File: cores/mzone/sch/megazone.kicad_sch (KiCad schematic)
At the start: 8 parts

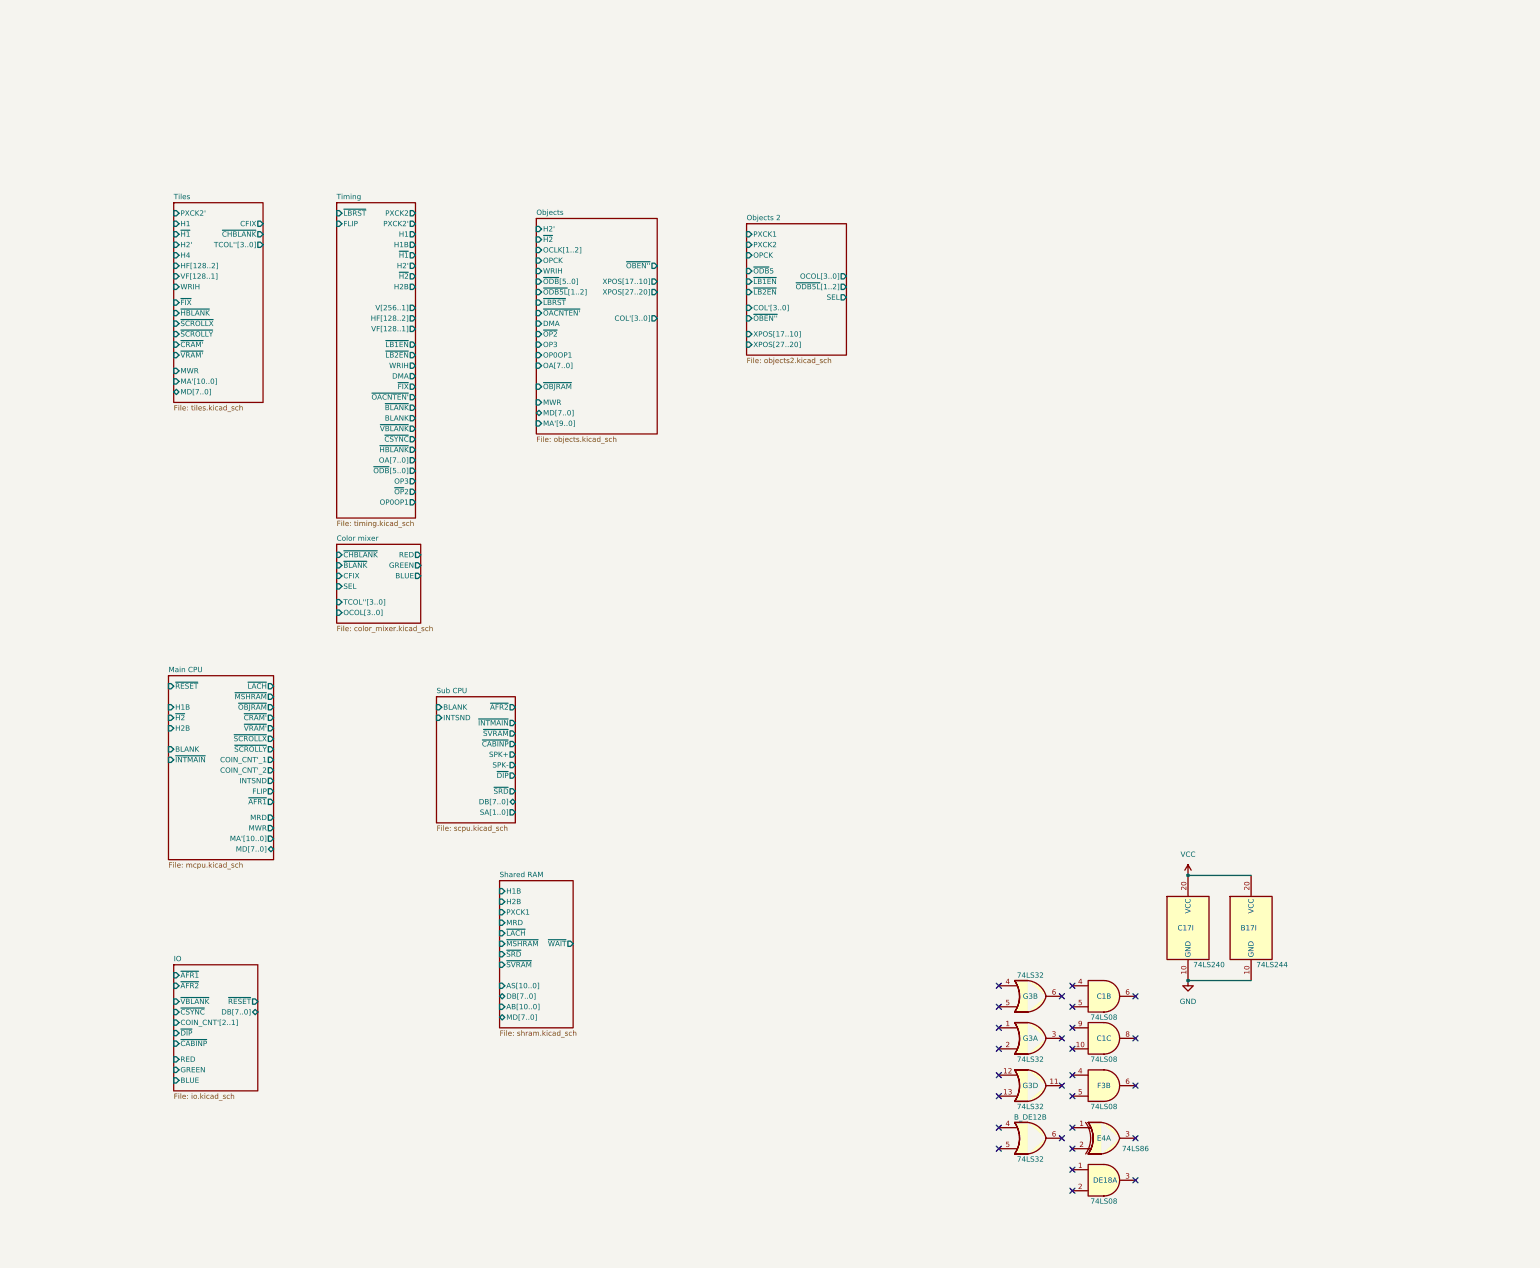
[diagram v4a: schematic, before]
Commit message: mzone core
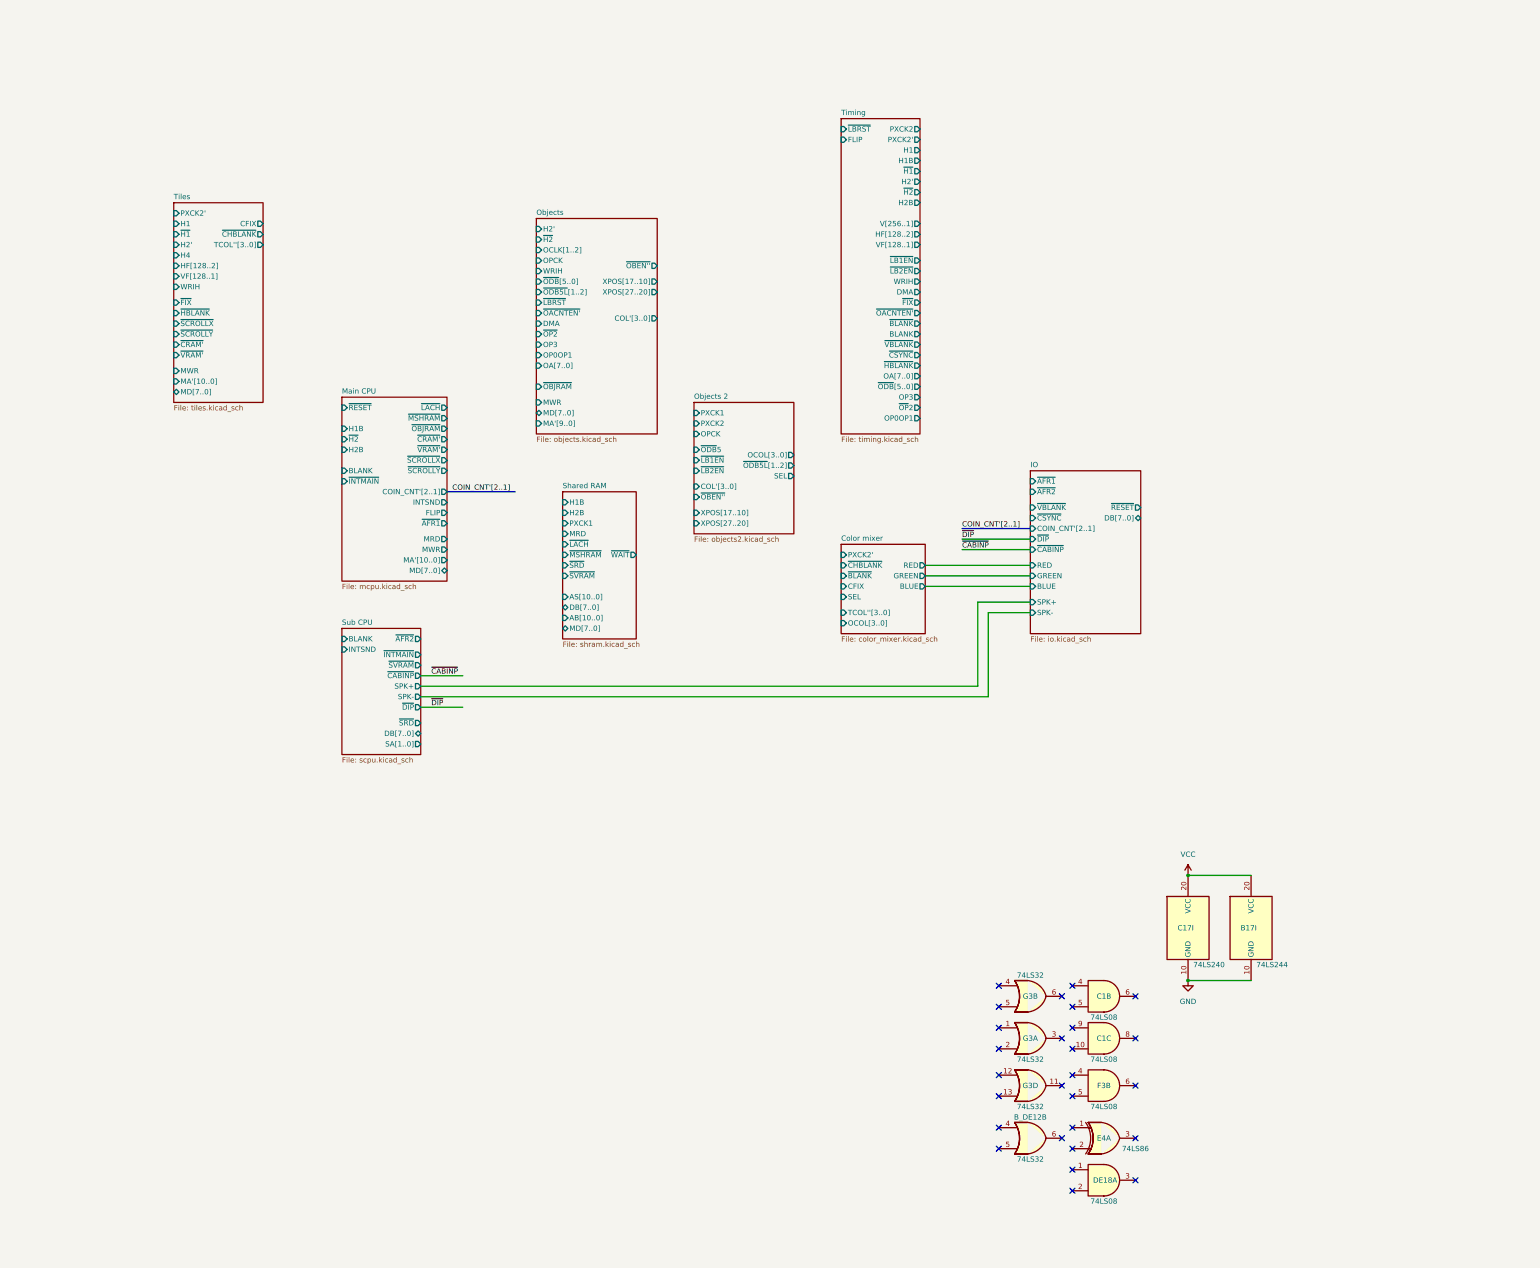
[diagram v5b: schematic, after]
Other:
- sheet Color mixer ports: added PXCK2'; removed none
- sheet IO ports: added SPK+, SPK-; removed none
- sheet Main CPU ports: added COIN_CNT'[2..1]; removed COIN_CNT'_1, COIN_CNT'_2

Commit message: mzone core
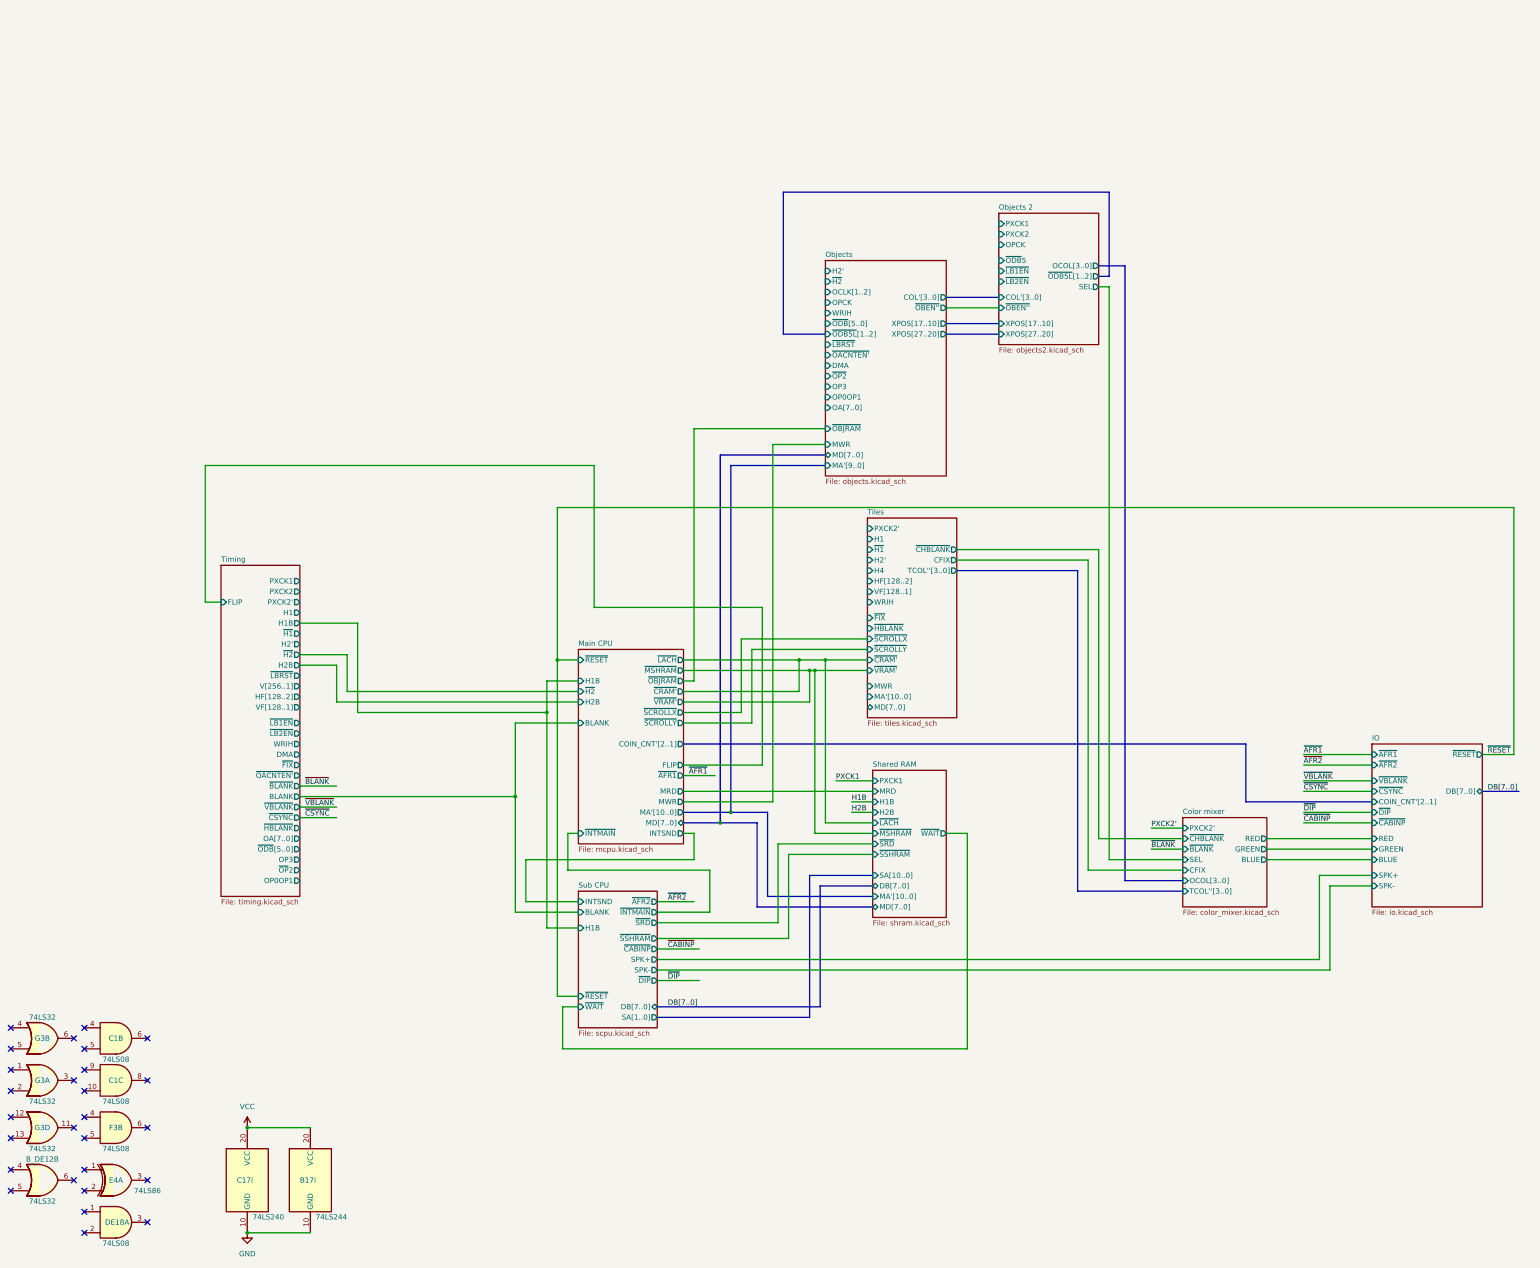
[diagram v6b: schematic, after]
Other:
- sheet Shared RAM ports: added MA'[10..0], SA[10..0], ~{SSHRAM}; removed AB[10..0], AS[10..0], ~{SVRAM}
- sheet Sub CPU ports: added H1B, ~{RESET}, ~{SSHRAM}, ~{WAIT}; removed ~{SVRAM}
- sheet Timing ports: added PXCK1; removed none
- moved on the sheet: B17I, B_DE12B, C17I, C1B, C1C, DE18A, E4A, F3B, G3A, G3B, G3D

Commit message: mzone core
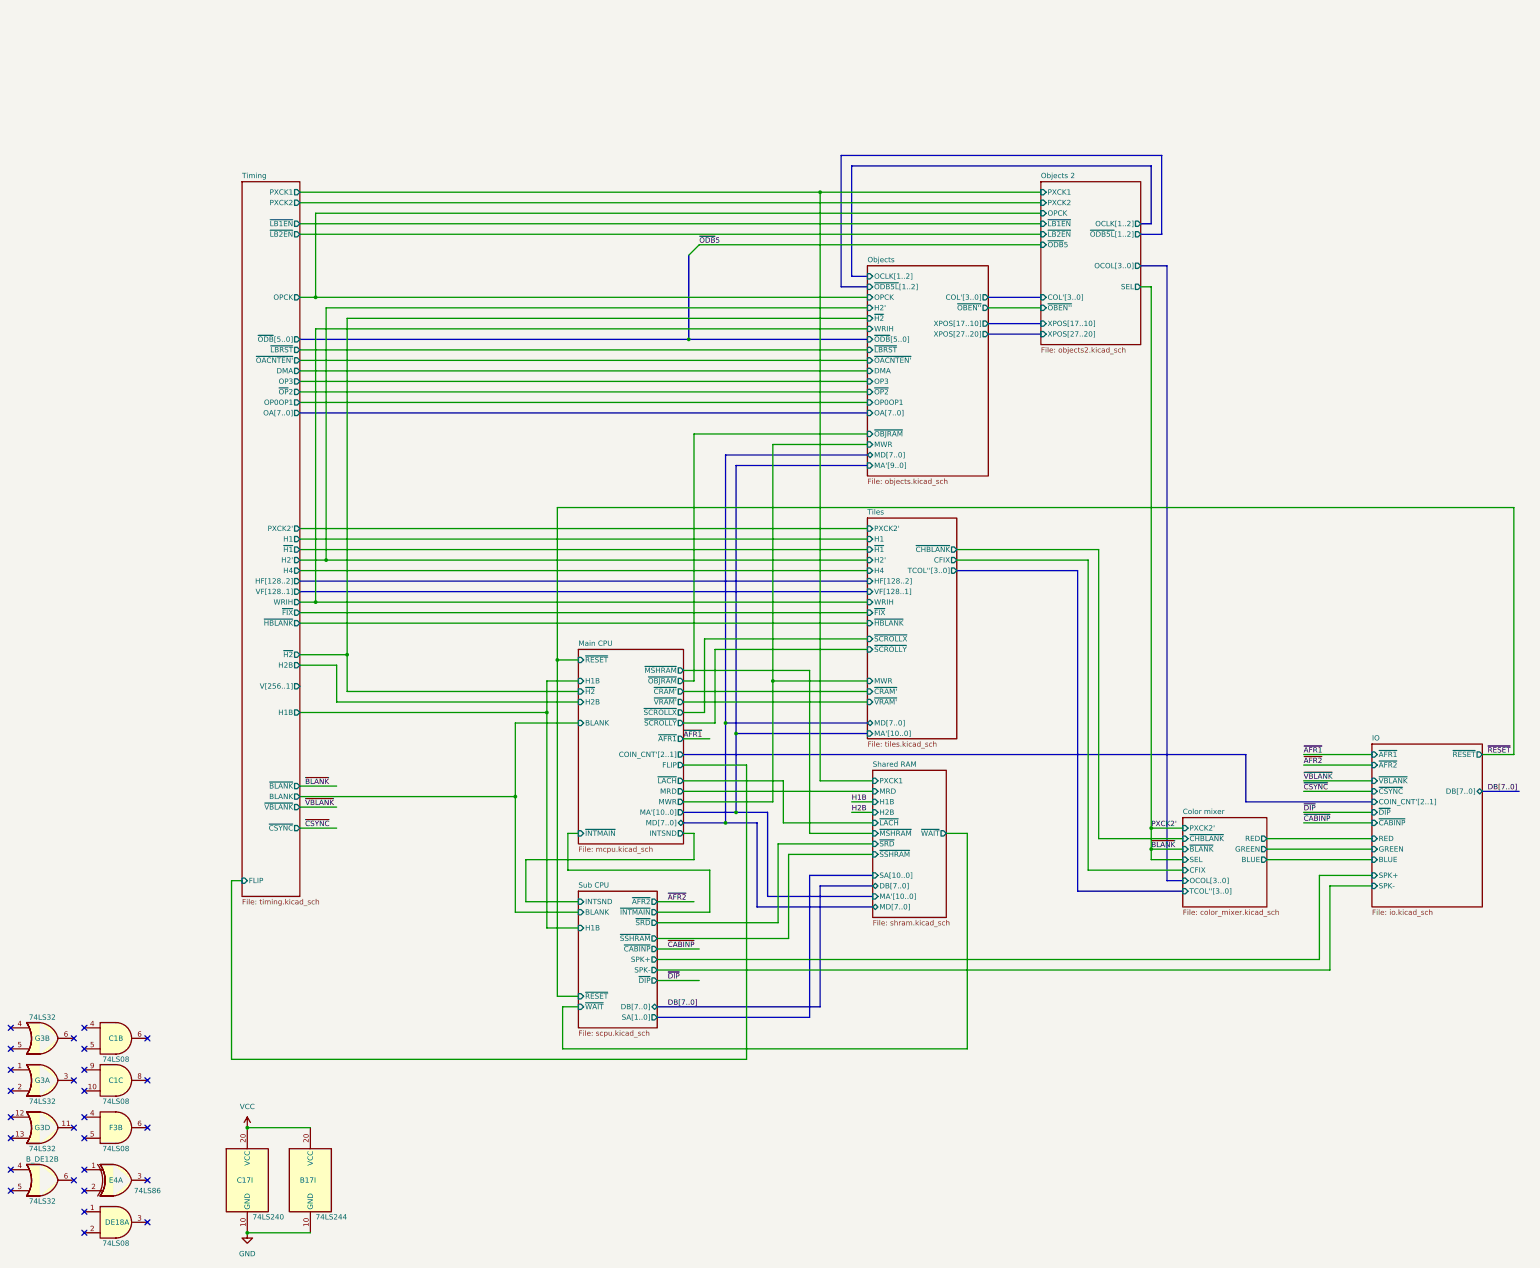
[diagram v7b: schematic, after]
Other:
- sheet Objects 2 ports: added OCLK[1..2]; removed none
- sheet Timing ports: added H4, OPCK; removed none

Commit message: mzone core
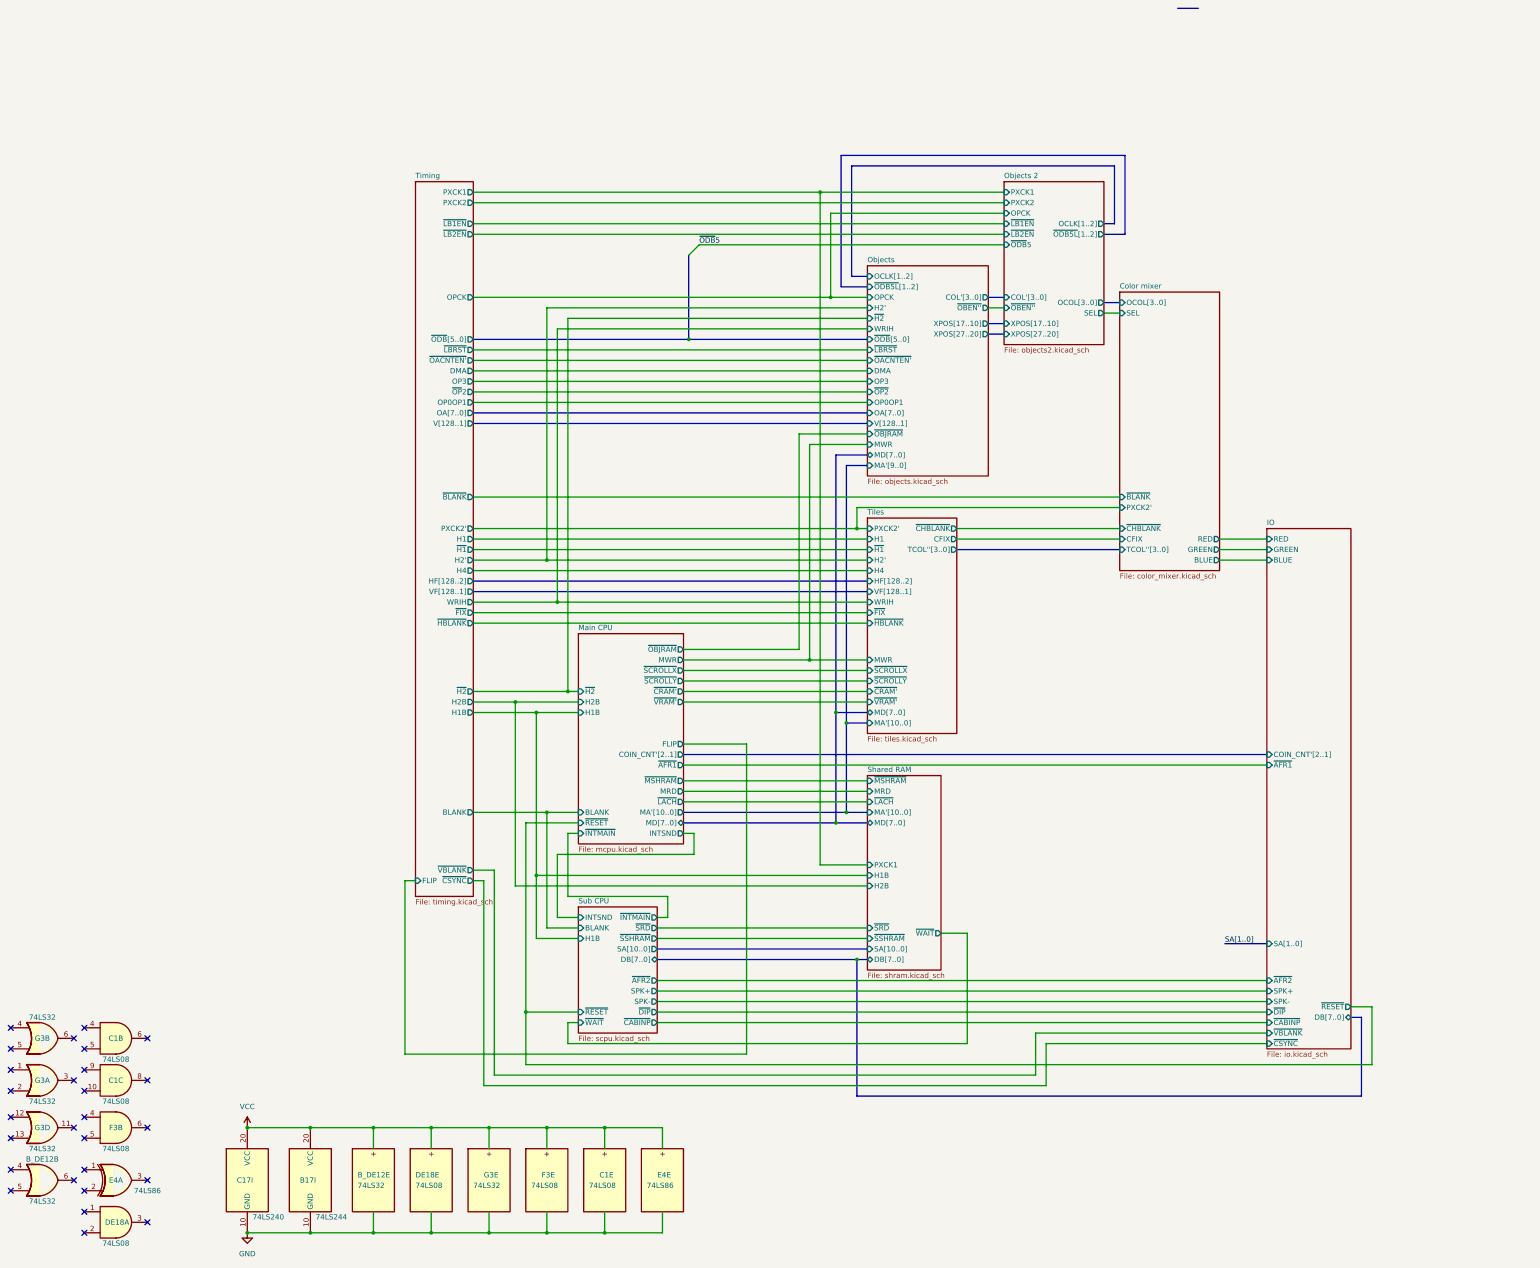
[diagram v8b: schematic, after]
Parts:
- added unit 5 of B_DE12
- added unit 5 of C1
- added unit 5 of DE18
- added unit 5 of E4
- added unit 5 of F3
- added unit 5 of G3
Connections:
- net GND: now also B_DE12.7 (GND), C1.7 (GND), DE18.7 (GND), E4.7 (GND), F3.7 (GND), G3.7 (GND)
- net VCC: now also B_DE12.14 (VCC), C1.14 (VCC), DE18.14 (VCC), E4.14 (VCC), F3.14 (VCC), G3.14 (VCC)
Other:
- sheet IO ports: added SA[1..0]; removed none
- sheet Objects ports: added V[128..1]; removed none
- sheet Sub CPU ports: added SA[10..0]; removed SA[1..0]
- sheet Timing ports: added V[128..1]; removed V[256..1]
